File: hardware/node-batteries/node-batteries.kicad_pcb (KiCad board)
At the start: 2 copper layers, 72.5 x 50 mm, 9 parts, among them J1 Conn_01x03_Male

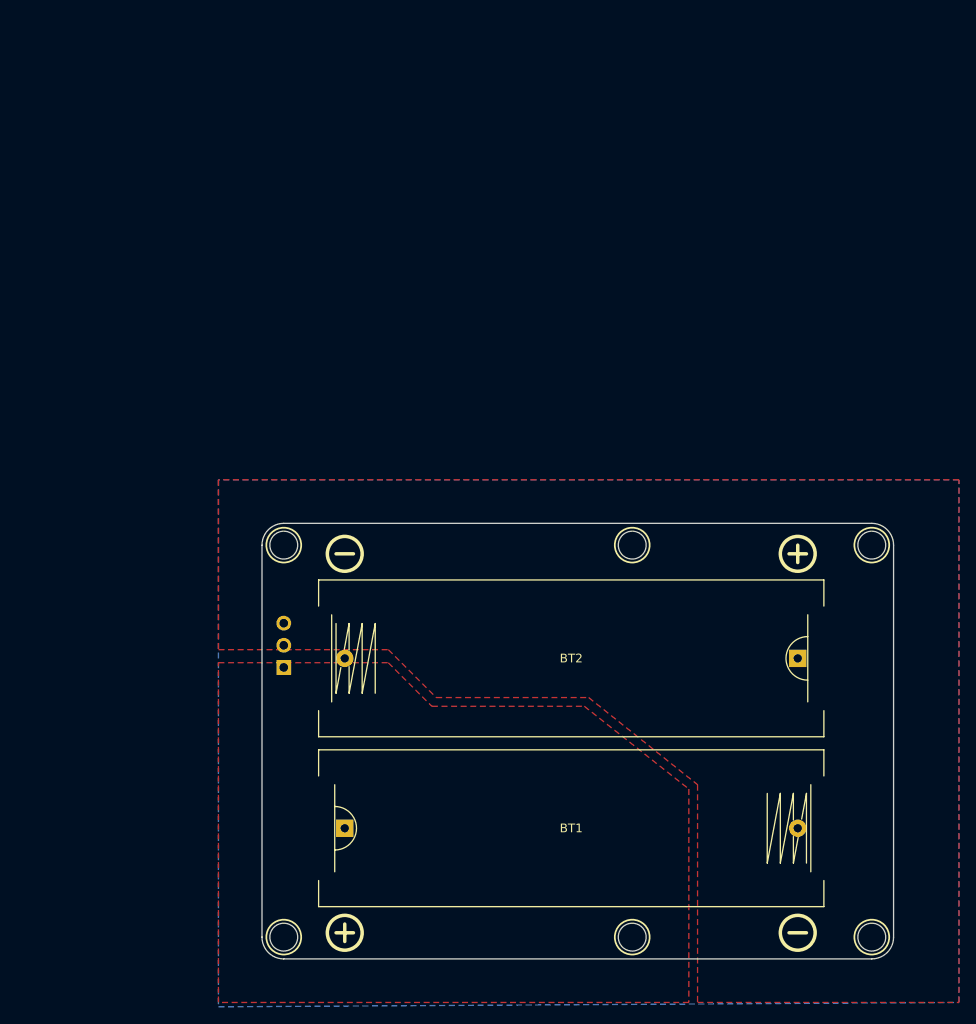
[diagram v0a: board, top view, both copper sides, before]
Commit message: Move power connector to other side
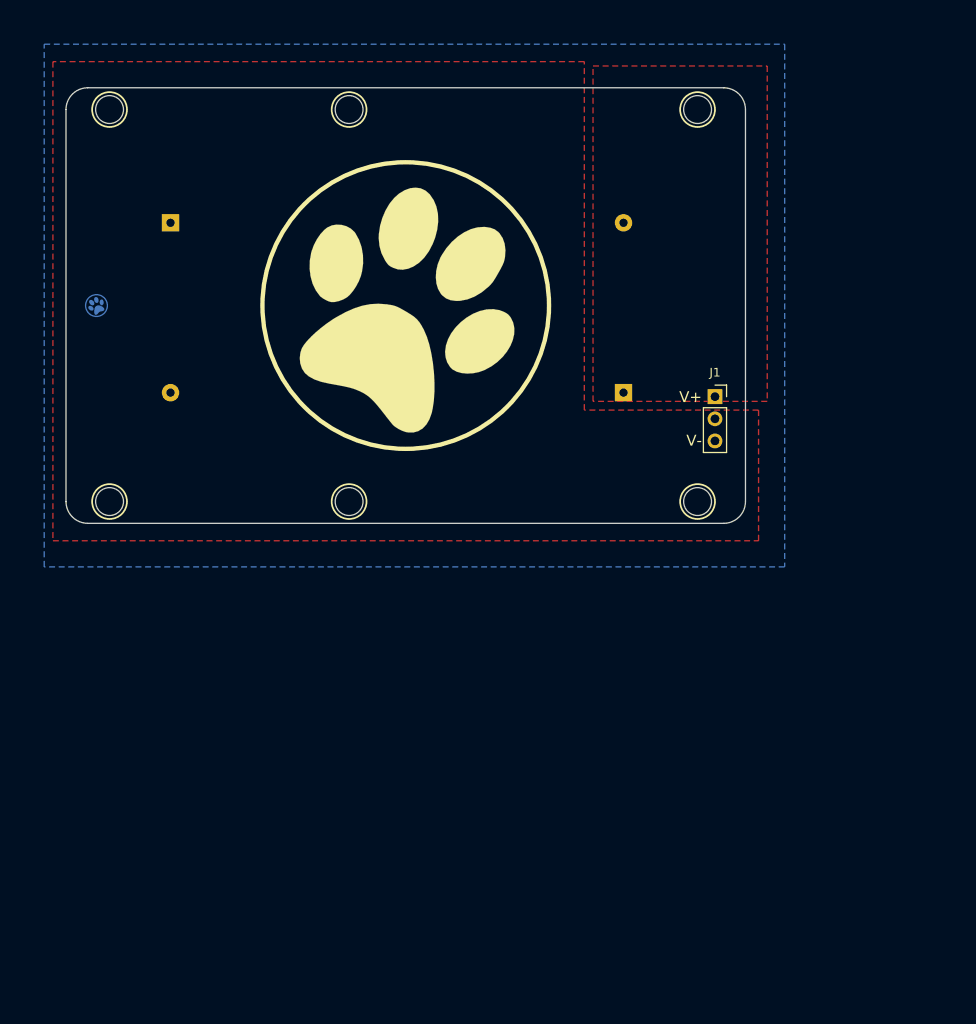
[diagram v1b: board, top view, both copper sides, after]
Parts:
- added G***: LOGO, humidity:paw-larger-screen, F.Cu at (66.5, 75.0)
- added G***: LOGO, humidity:paw-cu-circ, B.Cu at (31.0, 75.0)
- BT1, BT2: moved to B.Cu
- J1: moved to F.Cu
- moved MH2 59.6 mm to (60.0, 52.5)
- moved MH3 59.6 mm to (60.0, 97.5)
- moved J1 58.4 mm to (102.0, 85.5)
- moved BT1 53.9 mm to (65.5, 85.0), turned to 180 degrees
- moved BT2 53.9 mm to (65.5, 65.5), turned to 0 degrees
- moved MH1 53.9 mm to (32.5, 52.5)
- moved MH4 53.9 mm to (32.5, 97.5)
- moved MH5 53.9 mm to (100.0, 52.5)
- moved MH6 53.9 mm to (100.0, 97.5)
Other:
- board size 72.5 x 50 mm -> 78 x 50 mm
- board text added: "V+"
- board text added: "V-"

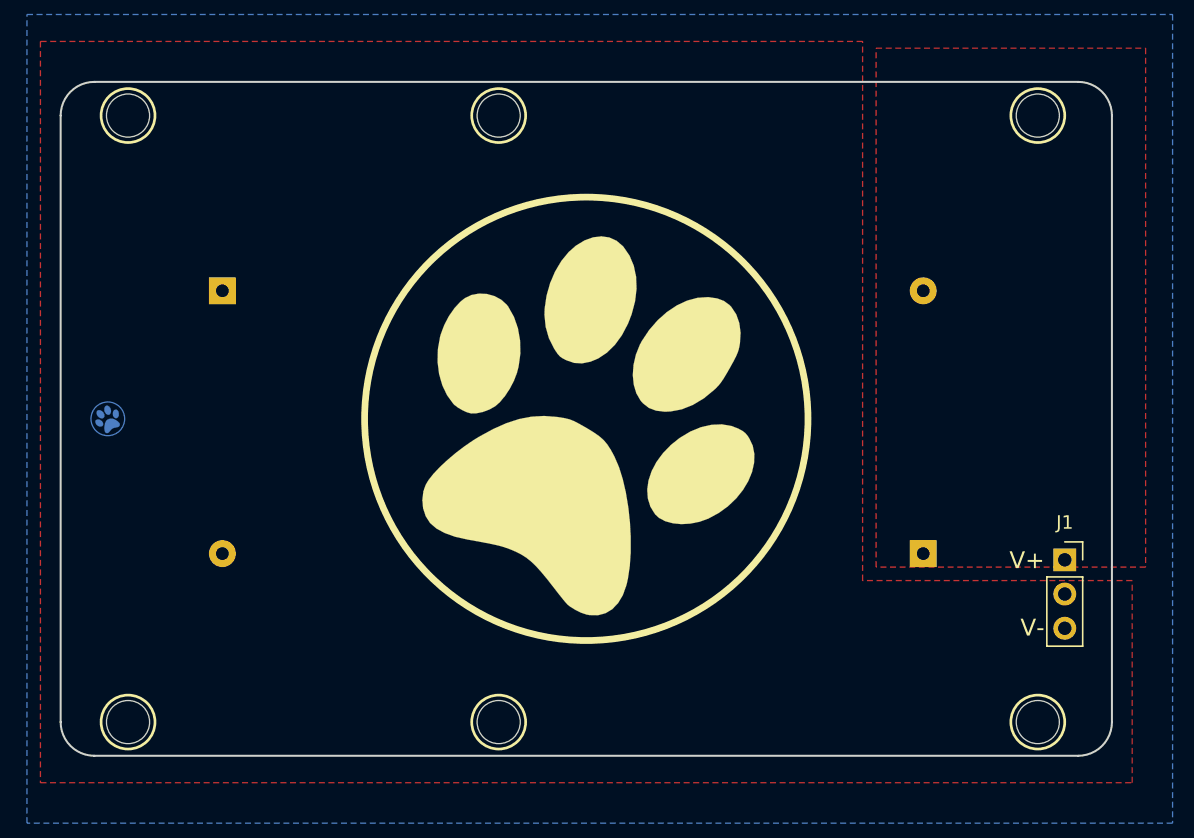
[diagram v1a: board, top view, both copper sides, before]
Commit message: Adjust mounting holes
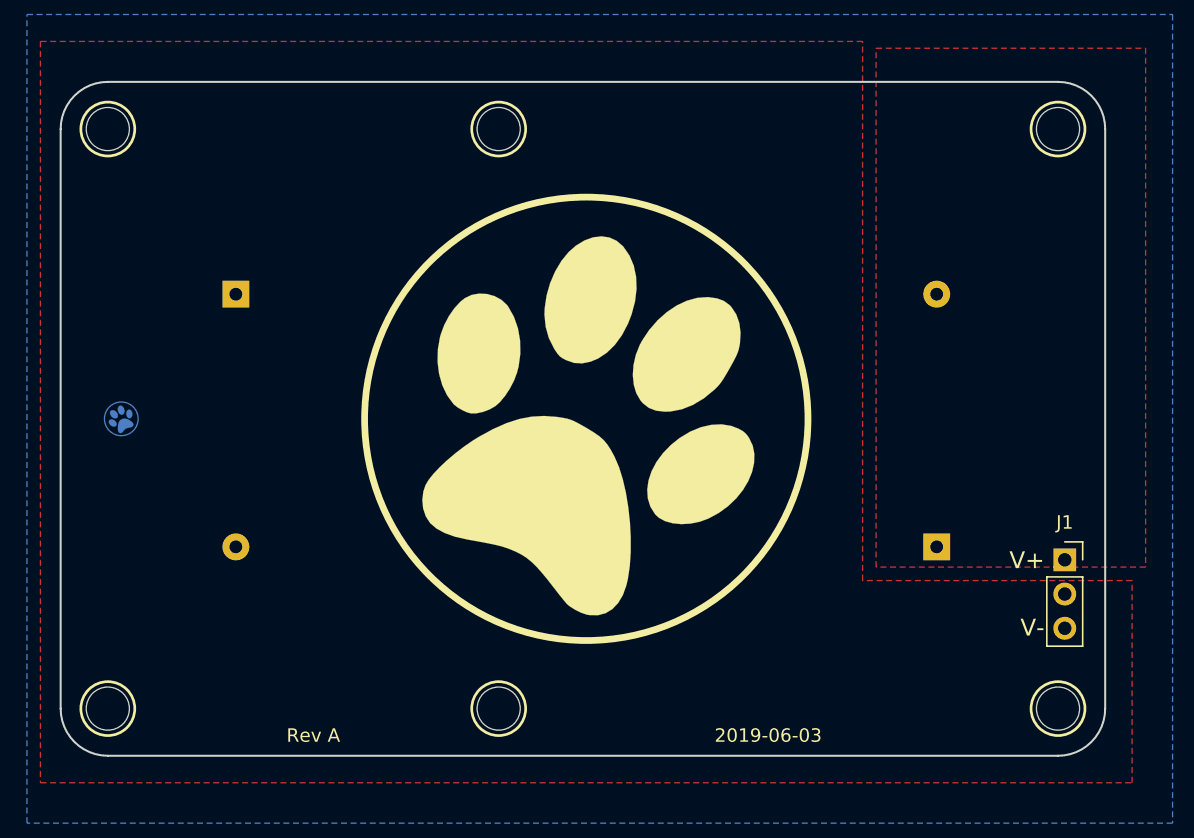
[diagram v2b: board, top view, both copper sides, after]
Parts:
- moved MH1 1.80 mm to (31.0, 53.5)
- moved MH4 1.80 mm to (31.0, 96.5)
- moved MH5 1.80 mm to (101.5, 53.5)
- moved MH6 1.80 mm to (101.5, 96.5)
- moved BT1 1.12 mm to (66.5, 84.5)
- moved BT2 1.03 mm to (66.5, 65.8)
- moved G*** 1.00 mm to (32.0, 75.0)
- moved MH2 1.00 mm to (60.0, 53.5)
- moved MH3 1.00 mm to (60.0, 96.5)
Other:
- board size 78 x 50 mm -> 77.5 x 50 mm
- board text added: "2019-06-03"
- board text added: "Rev A"

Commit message: Added missing file
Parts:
- moved MH1 2.50 mm to (33.5, 53.5)
- moved MH4 2.50 mm to (33.5, 96.5)
- moved G*** 1.25 mm to (33.2, 75.0)
- moved BT1 1.00 mm to (67.5, 84.5)
- moved BT2 1.00 mm to (67.5, 65.8)
- moved G*** 1.00 mm to (67.5, 75.0)
- moved J1 0.50 mm to (101.5, 85.5)
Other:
- board size 77.5 x 50 mm -> 75 x 50 mm
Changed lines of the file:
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@@
   )
   (module humidity:AA_Battery_Holder (layer B.Cu)
-    (at 66.5 84.5 180)
+    (at 67.5 84.5 180)
     (fp_text reference BT1 (at 0 0 180) (layer B.SilkS)
       (effects (font (size 1 1) (thickness 0.15)) (justify mirror))
@@
   )
   (module humidity:AA_Battery_Holder (layer B.Cu)
-    (at 66.5 65.75)
+    (at 67.5 65.75)
     (fp_text reference BT2 (at 0 0) (layer B.SilkS)
       (effects (font (size 1 1) (thickness 0.15)) (justify mirror))
@@
   )
   (module MountingHole:MountingHole_3.2mm_M3 locked (layer F.Cu)
-    (at 31 53.5)
+    (at 33.5 53.5)
     (descr "Mounting Hole 3.2mm, no annular, M3")
     (tags "mounting hole 3.2mm no annular m3")
@@
   )
   (module MountingHole:MountingHole_3.2mm_M3 locked (layer F.Cu)
-    (at 31 96.5)
+    (at 33.5 96.5)
     (descr "Mounting Hole 3.2mm, no annular, M3")
     (tags "mounting hole 3.2mm no annular m3")
@@
   )
   (module Connector_PinSocket_2.54mm:PinSocket_1x03_P2.54mm_Vertical (layer F.Cu)
-    (at 102 85.46)
+    (at 101.5 85.46)
     (descr "Through hole straight socket strip, 1x03, 2.54mm pitch, single row (from Kicad 4.0.7), script generated")
     (tags "Through hole socket strip THT 1x03 2.54mm single row")
@@
   )
   (module humidity:paw-larger-screen (layer F.Cu)
-    (at 66.5 75 330)
+    (at 67.5 75 330)
     (fp_text reference G*** (at 0 0 330) (layer F.SilkS) hide
       (effects (font (size 1.524 1.524) (thickness 0.3)))
@@
   )
   (module humidity:paw-cu-circ (layer B.Cu)
-    (at 32 75 210)
+    (at 33.25 75 210)
     (fp_text reference G*** (at 0 0 210) (layer B.SilkS) hide
       (effects (font (size 1.524 1.524) (thickness 0.3)) (justify mirror))
@@
     (effects (font (size 1 1) (thickness 0.2)))
   )
-  (gr_circle (center 31 53.5) (end 33 53.5) (layer B.SilkS) (width 0.2))
+  (gr_circle (center 33.5 53.5) (end 35.5 53.5) (layer B.SilkS) (width 0.2))
   (gr_circle (center 60 53.5) (end 62 53.5) (layer B.SilkS) (width 0.2))
   (gr_circle (center 101.5 53.5) (end 103.5 53.5) (layer B.SilkS) (width 0.2))
   (gr_circle (center 101.5 96.5) (end 99.5 96.5) (layer B.SilkS) (width 0.2))
   (gr_circle (center 60 96.5) (end 62 96.5) (layer B.SilkS) (width 0.2))
-  (gr_circle (center 31 96.5) (end 33 96.5) (layer B.SilkS) (width 0.2))
-  (gr_circle (center 66.5 75) (end 82.948784 75) (layer F.SilkS) (width 0.5))
-  (gr_line (start 66.5 50) (end 66.5 100) (layer Eco1.User) (width 0.2))
-  (gr_line (start 91.5 96) (end 91.5 98) (layer B.SilkS) (width 0.4))
-  (gr_text V- (at 100.5 90.5) (layer B.SilkS)
+  (gr_circle (center 33.5 96.5) (end 35.5 96.5) (layer B.SilkS) (width 0.2))
+  (gr_circle (center 67.551216 75) (end 84 75) (layer F.SilkS) (width 0.5))
+  (gr_line (start 67.5 50) (end 67.5 100) (layer Eco1.User) (width 0.2))
+  (gr_line (start 93.5 96) (end 93.5 98) (layer B.SilkS) (width 0.4))
+  (gr_text V- (at 100 90.5) (layer B.SilkS)
     (effects (font (size 1.25 1.25) (thickness 0.3)) (justify left mirror))
   )
-  (gr_text V+ (at 100.5 85.5) (layer B.SilkS)
+  (gr_text V+ (at 100 85.5) (layer B.SilkS)
     (effects (font (size 1.25 1.25) (thickness 0.3)) (justify left mirror))
   )
-  (dimension 29 (width 0.3) (layer Eco1.User)
-    (gr_text "29,000 mm" (at 45.5 39.9) (layer Eco1.User)
+  (dimension 26.5 (width 0.3) (layer Eco1.User)
+    (gr_text "26,500 mm" (at 46.75 39.9) (layer Eco1.User)
       (effects (font (size 1.5 1.5) (thickness 0.3)))
     )
-    (feature1 (pts (xy 31 50) (xy 31 41.413579)))
+    (feature1 (pts (xy 33.5 50) (xy 33.5 41.413579)))
     (feature2 (pts (xy 60 50) (xy 60 41.413579)))
-    (crossbar (pts (xy 60 42) (xy 31 42)))
-    (arrow1a (pts (xy 31 42) (xy 32.126504 41.413579)))
-    (arrow1b (pts (xy 31 42) (xy 32.126504 42.586421)))
+    (crossbar (pts (xy 60 42) (xy 33.5 42)))
+    (arrow1a (pts (xy 33.5 42) (xy 34.626504 41.413579)))
+    (arrow1b (pts (xy 33.5 42) (xy 34.626504 42.586421)))
     (arrow2a (pts (xy 60 42) (xy 58.873496 41.413579)))
     (arrow2b (pts (xy 60 42) (xy 58.873496 42.586421)))
@@
     (arrow2b (pts (xy 117 100) (xy 116.413579 98.873496)))
   )
-  (dimension 77.5 (width 0.3) (layer Eco1.User)
-    (gr_text "77,500 mm" (at 66.25 35.4) (layer Eco1.User)
+  (dimension 75 (width 0.3) (layer Eco1.User)
+    (gr_text "75,000 mm" (at 67.5 35.4) (layer Eco1.User)
       (effects (font (size 1.5 1.5) (thickness 0.3)))
     )
     (feature1 (pts (xy 105 50) (xy 105 36.913579)))
-    (feature2 (pts (xy 27.5 50) (xy 27.5 36.913579)))
-    (crossbar (pts (xy 27.5 37.5) (xy 105 37.5)))
+    (feature2 (pts (xy 30 50) (xy 30 36.913579)))
+    (crossbar (pts (xy 30 37.5) (xy 105 37.5)))
     (arrow1a (pts (xy 105 37.5) (xy 103.873496 38.086421)))
     (arrow1b (pts (xy 105 37.5) (xy 103.873496 36.913579)))
-    (arrow2a (pts (xy 27.5 37.5) (xy 28.626504 38.086421)))
-    (arrow2b (pts (xy 27.5 37.5) (xy 28.626504 36.913579)))
-  )
-  (gr_text V+ (at 100.5 85.5) (layer F.SilkS)
+    (arrow2a (pts (xy 30 37.5) (xy 31.126504 38.086421)))
+    (arrow2b (pts (xy 30 37.5) (xy 31.126504 36.913579)))
+  )
+  (gr_text V+ (at 100 85.5) (layer F.SilkS)
     (effects (font (size 1.25 1.25) (thickness 0.3)) (justify right))
   )
-  (gr_text V- (at 100.5 90.5) (layer F.SilkS)
+  (gr_text V- (at 100 90.5) (layer F.SilkS)
     (effects (font (size 1.25 1.25) (thickness 0.3)) (justify right))
   )
-  (gr_circle (center 39.5 97) (end 41.5 97) (layer B.SilkS) (width 0.4))
-  (gr_line (start 38.5 97) (end 40.5 97) (layer B.SilkS) (width 0.4))
-  (gr_circle (center 91.5 97) (end 93.5 97) (layer B.SilkS) (width 0.4))
-  (gr_line (start 90.5 97) (end 92.5 97) (layer B.SilkS) (width 0.4))
-  (gr_line (start 38.5 53.5) (end 40.5 53.5) (layer B.SilkS) (width 0.4))
-  (gr_line (start 39.5 52.5) (end 39.5 54.5) (layer B.SilkS) (width 0.4))
-  (gr_circle (center 39.5 53.5) (end 41.5 53.5) (layer B.SilkS) (width 0.4))
-  (gr_line (start 90.5 53.5) (end 92.5 53.5) (layer B.SilkS) (width 0.4))
-  (gr_circle (center 91.5 53.5) (end 93.5 53.5) (layer B.SilkS) (width 0.4))
-  (gr_circle (center 31 96.5) (end 33 96.5) (layer F.SilkS) (width 0.2))
-  (gr_circle (center 31 53.5) (end 33 53.5) (layer F.SilkS) (width 0.2))
+  (gr_circle (center 41.5 97) (end 43.5 97) (layer B.SilkS) (width 0.4))
+  (gr_line (start 40.5 97) (end 42.5 97) (layer B.SilkS) (width 0.4))
+  (gr_circle (center 93.5 97) (end 95.5 97) (layer B.SilkS) (width 0.4))
+  (gr_line (start 92.5 97) (end 94.5 97) (layer B.SilkS) (width 0.4))
+  (gr_line (start 40.5 53) (end 42.5 53) (layer B.SilkS) (width 0.4))
+  (gr_line (start 41.5 52) (end 41.5 54) (layer B.SilkS) (width 0.4))
+  (gr_circle (center 41.5 53) (end 43.5 53) (layer B.SilkS) (width 0.4))
+  (gr_line (start 92.5 53) (end 94.5 53) (layer B.SilkS) (width 0.4))
+  (gr_circle (center 93.5 53) (end 95.5 53) (layer B.SilkS) (width 0.4))
+  (gr_circle (center 33.5 96.5) (end 35.5 96.5) (layer F.SilkS) (width 0.2))
+  (gr_circle (center 33.5 53.5) (end 35.5 53.5) (layer F.SilkS) (width 0.2))
   (gr_circle (center 60 53.5) (end 62 53.5) (layer F.SilkS) (width 0.2))
   (gr_circle (center 101.5 53.5) (end 103.5 53.5) (layer F.SilkS) (width 0.2))
   (gr_circle (center 101.5 96.5) (end 103.5 96.5) (layer F.SilkS) (width 0.2))
-  (gr_line (start 105.5 75) (end 27.5 75) (layer Eco1.User) (width 0.15))
+  (gr_line (start 105.5 75) (end 30 75) (layer Eco1.User) (width 0.15))
   (gr_arc (start 101.5 96.5) (end 101.5 100) (angle -90) (layer Edge.Cuts) (width 0.15))
   (gr_arc (start 101.5 53.5) (end 105 53.5) (angle -90) (layer Edge.Cuts) (width 0.15))
   (gr_line (start 105 53.5) (end 105 96.5) (layer Edge.Cuts) (width 0.15))
-  (gr_line (start 31 50) (end 101.5 50) (layer Edge.Cuts) (width 0.15))
-  (gr_line (start 31 100) (end 101.5 100) (layer Edge.Cuts) (width 0.15))
-  (gr_line (start 27.5 53.5) (end 27.5 96.5) (layer Edge.Cuts) (width 0.15))
-  (gr_arc (start 31 53.5) (end 31 50) (angle -90) (layer Edge.Cuts) (width 0.15))
-  (gr_arc (start 31 96.5) (end 27.5 96.5) (angle -90) (layer Edge.Cuts) (width 0.15))
+  (gr_line (start 33.5 50) (end 101.5 50) (layer Edge.Cuts) (width 0.15))
+  (gr_line (start 33.5 100) (end 101.5 100) (layer Edge.Cuts) (width 0.15))
+  (gr_line (start 30 53.5) (end 30 96.5) (layer Edge.Cuts) (width 0.15))
+  (gr_arc (start 33.5 53.5) (end 33.5 50) (angle -90) (layer Edge.Cuts) (width 0.15))
+  (gr_arc (start 33.5 96.5) (end 30 96.5) (angle -90) (layer Edge.Cuts) (width 0.15))
   (gr_circle (center 60 96.5) (end 62 96.5) (layer F.SilkS) (width 0.2))
   (zone (net 3) (net_name /GND) (layer B.Cu) (hatch edge 0.508)
